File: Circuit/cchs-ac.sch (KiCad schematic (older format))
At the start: 17 parts

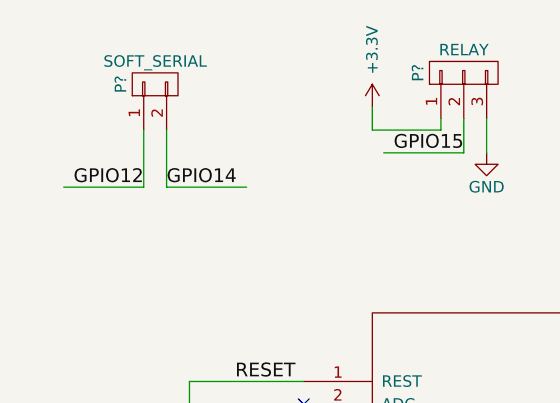
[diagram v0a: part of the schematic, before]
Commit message: Removed Software Serial Pins
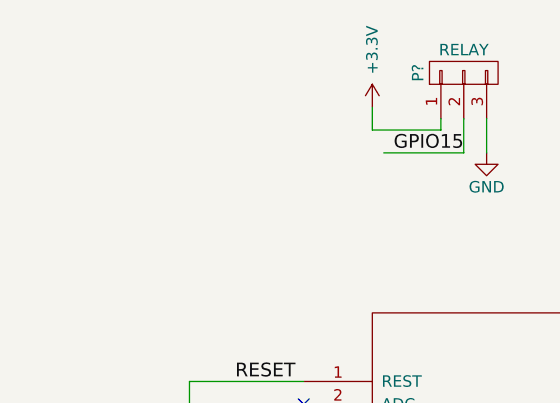
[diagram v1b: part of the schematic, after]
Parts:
- removed P?: SOFT_SERIAL, symbol CONN_01X02
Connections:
- wire segments 59 -> 55
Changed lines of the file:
@@
 Connection ~ 6050 4850
-$Comp
-L CONN_01X02 P?
-U 1 1 566AF1DB
-P 3300 1450
-F 0 "P?" H 3300 1600 50  0000 C CNN
-F 1 "SOFT_SERIAL" V 3400 1450 50  0000 C CNN
-F 2 "" H 3300 1450 60  0000 C CNN
-F 3 "" H 3300 1450 60  0000 C CNN
-	1    3300 1450
-	0    -1   -1   0
-$EndComp
-Wire Wire Line
-	3350 1650 3350 1900
-Text Label 3350 1900 0    60   ~ 0
-GPIO14
-Text Label 3250 1900 2    60   ~ 0
-GPIO12
-Wire Wire Line
-	3350 1900 3700 1900
-Wire Wire Line
-	3250 1650 3250 1900
-Wire Wire Line
-	3250 1900 2900 1900
 $Comp
 L CONN_01X03 P?
